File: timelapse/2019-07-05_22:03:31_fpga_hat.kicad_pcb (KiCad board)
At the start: 4 copper layers, 65 x 56.5 mm, 91 parts, among them J1 2x20, J2 AudioJack3, J3 Conn_02x06_Top_Bottom, J4 Conn_02x06_Top_Bottom, J5 Conn_02x06_Top_Bottom, J6 Conn_01x02, SW1 PTS815, SW2 PTS815, SW3 PTS815, SW4 PTS815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

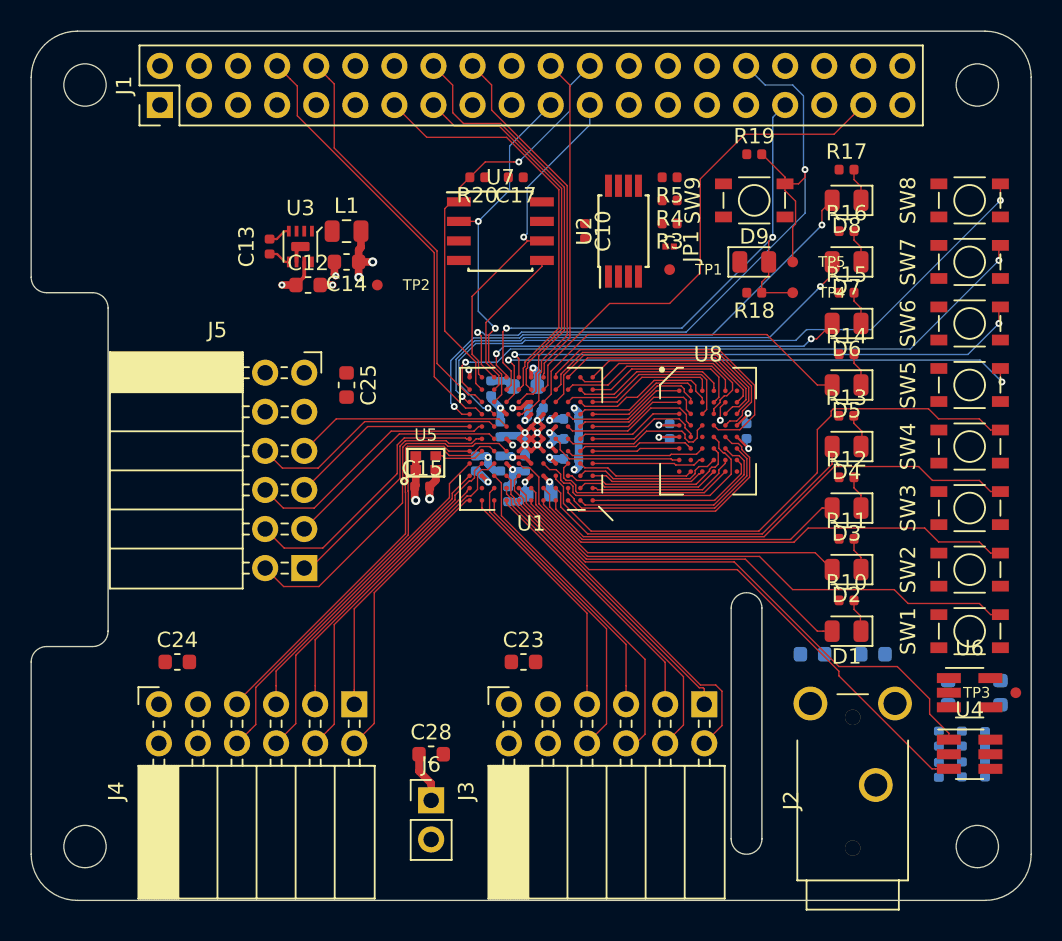
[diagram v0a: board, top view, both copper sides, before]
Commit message: Connect up SDIO, remaining buttons + LEDs.
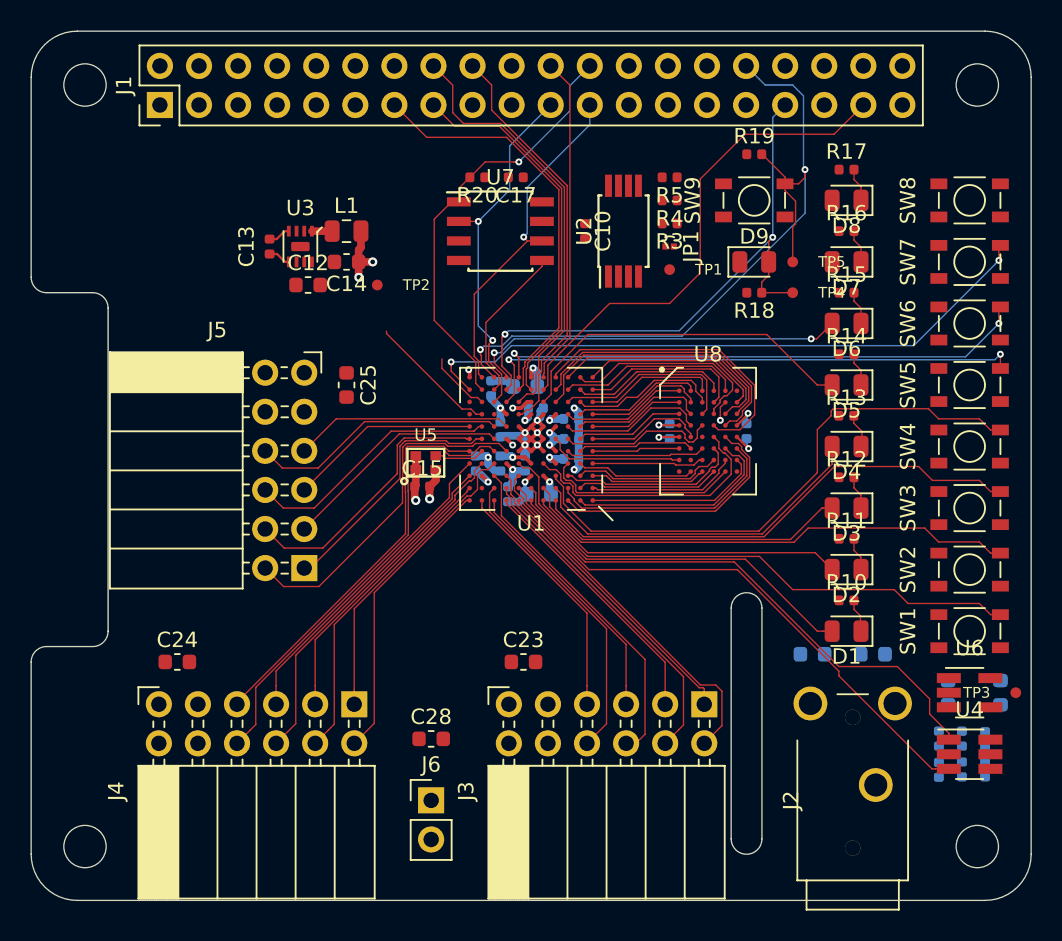
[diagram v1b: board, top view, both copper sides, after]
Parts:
- moved C28 1.00 mm to (126.0, 126.0)
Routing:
- net /SW7: track 45.2 -> 0.00 mm, vias 2 -> 0
- net /LED7: track 33.9 -> 0.00 mm, vias 2 -> 0
- net /LED6: track 30.8 -> 0.00 mm, vias 2 -> 0
- net /GP15_UART_RXD: track 26.5 -> 4.12 mm
- net /GP14_UART_TXD: track 28.5 -> 8.53 mm
- net +5V: track 5.96 -> 0.00 mm, vias 1 -> 0
- net GND: track 33.0 -> 30.2 mm, vias 14 -> 12
- net Net-(L1-Pad1): track 0.00 -> 1.31 mm
- net /SW6: track 40.5 -> 41.6 mm
- net /GP12_FPGA_~RST: track 50.2 -> 49.1 mm
- net /GP8_SPI_~CS: track 27.5 -> 28.1 mm
- net /SW4: track 36.7 -> 36.1 mm
